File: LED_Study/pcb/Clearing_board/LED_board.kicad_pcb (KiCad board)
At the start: 2 copper layers, 8 x 8 mm, 4 parts

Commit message: new boards
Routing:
- added copper zone on F.Cu, net /GND
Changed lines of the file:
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@@
   (segment (start 102.5 100) (end 102.5 102.05) (width 0.5) (layer "F.Cu") (net 4))
   (via (at 102.5 100) (size 1.4) (drill 0.8) (layers "F.Cu" "B.Cu") (net 4))
+  (zone (net 4) (net_name "/GND") (layer "F.Cu") (hatch edge 0.5)
+    (connect_pads (clearance 0.5))
+    (min_thickness 0.25) (filled_areas_thickness no)
+    (fill yes (thermal_gap 0.5) (thermal_bridge_width 0.5))
+    (polygon
+      (pts
+        (xy 96 96)
+        (xy 104 96)
+        (xy 104 104)
+        (xy 96 104)
+      )
+    )
+  )
 )

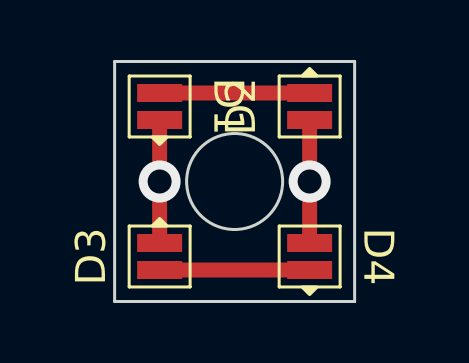
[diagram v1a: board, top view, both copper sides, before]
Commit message: updated boards and ordered from PCBway
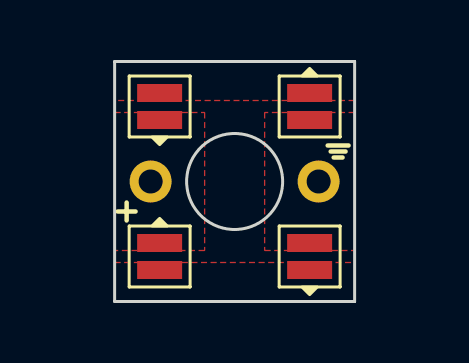
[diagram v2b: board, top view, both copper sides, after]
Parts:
- added J1: Conn_01x01_Pin, Connector_PinHeader_1.00mm:PinHeader_1x01_P1.00mm_Vertical, F.Cu at (97.2, 100.0)
- added J2: Conn_01x01_Pin, Connector_PinHeader_1.00mm:PinHeader_1x01_P1.00mm_Vertical, F.Cu at (102.8, 100.0)
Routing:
- net Net-(D3-K): track 5.00 -> 0.00 mm
- net Net-(D1-K): track 5.00 -> 0.00 mm
- net /Vin: track 4.10 -> 0.00 mm, vias 1 -> 0
- net /GND: track 4.10 -> 0.00 mm, vias 1 -> 0
- added copper zone on F.Cu, net /Vin
- added copper zone on F.Cu, net Net-(D1-K)
- added copper zone on F.Cu, net Net-(D3-K)
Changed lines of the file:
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@@
   (net 3 "/Vin")
   (net 4 "/GND")
+  (footprint "Connector_PinHeader_1.00mm:PinHeader_1x01_P1.00mm_Vertical" (layer "F.Cu")
+    (at 102.8 100)
+    (descr "Through hole straight pin header, 1x01, 1.00mm pitch, single row")
+    (tags "Through hole pin header THT 1x01 1.00mm single row")
+    (property "Sheetfile" "LED_board.kicad_sch")
+    (property "Sheetname" "")
+    (property "ki_description" "Generic connector, single row, 01x01, script generated")
+    (property "ki_keywords" "connector")
+    (attr through_hole)
+    (fp_text reference "J2" (at 0 -1.56) (layer "F.SilkS") hide
+        (effects (font (size 1 1) (thickness 0.15)))
+    )
+    (fp_text value "Conn_01x01_Pin" (at 0 1.56) (layer "F.Fab")
+        (effects (font (size 1 1) (thickness 0.15)))
+    )
+    (fp_text user "${REFERENCE}" (at 0 0 90) (layer "F.Fab")
+        (effects (font (size 0.76 0.76) (thickness 0.114)))
+    )
+    (fp_line (start -1.15 -1) (end -1.15 1)
+      (stroke (width 0.05) (type solid)) (layer "F.CrtYd"))
+    (fp_line (start -1.15 1) (end 1.15 1)
+      (stroke (width 0.05) (type solid)) (layer "F.CrtYd"))
+    (fp_line (start 1.15 -1) (end -1.15 -1)
+      (stroke (width 0.05) (type solid)) (layer "F.CrtYd"))
+    (fp_line (start 1.15 1) (end 1.15 -1)
+      (stroke (width 0.05) (type solid)) (layer "F.CrtYd"))
+    (fp_line (start -0.635 -0.1825) (end -0.3175 -0.5)
+      (stroke (width 0.1) (type solid)) (layer "F.Fab"))
+    (fp_line (start -0.635 0.5) (end -0.635 -0.1825)
+      (stroke (width 0.1) (type solid)) (layer "F.Fab"))
+    (fp_line (start -0.3175 -0.5) (end 0.635 -0.5)
+      (stroke (width 0.1) (type solid)) (layer "F.Fab"))
+    (fp_line (start 0.635 -0.5) (end 0.635 0.5)
+      (stroke (width 0.1) (type solid)) (layer "F.Fab"))
+    (fp_line (start 0.635 0.5) (end -0.635 0.5)
+      (stroke (width 0.1) (type solid)) (layer "F.Fab"))
+    (pad "1" thru_hole circle (at 0 0) (size 1.4 1.4) (drill 0.8) (layers "*.Cu" "*.Mask")
+      (net 4 "/GND") (pinfunction "Pin_1") (pintype "passive"))
+    (model "${KICAD6_3DMODEL_DIR}/Connector_PinHeader_1.00mm.3dshapes/PinHeader_1x01_P1.00mm_Vertical.wrl"
+      (offset (xyz 0 0 0))
+      (scale (xyz 1 1 1))
+      (rotate (xyz 0 0 0))
+    )
+  )
   (footprint "SST-10-IRD-B130-S940:XQE" (layer "F.Cu")
     (at 97.5 102.5 90)
@@
     (property "ki_keywords" "LED diode")
     (attr smd)
-    (fp_text reference "D3" (at 0 -2.286 90 unlocked) (layer "F.SilkS")
+    (fp_text reference "D3" (at 0 -2.286 90 unlocked) (layer "F.SilkS") hide
         (effects (font (size 1 1) (thickness 0.1)))
     )
@@
     (property "ki_keywords" "LED diode")
     (attr smd)
-    (fp_text reference "D1" (at 0 -2.286 -90 unlocked) (layer "F.SilkS")
+    (fp_text reference "D1" (at 0 -2.286 -90 unlocked) (layer "F.SilkS") hide
         (effects (font (size 1 1) (thickness 0.1)))
     )
@@
     (property "ki_keywords" "LED diode")
     (attr smd)
-    (fp_text reference "D4" (at 0 -2.286 -90 unlocked) (layer "F.SilkS")
+    (fp_text reference "D4" (at 0 -2.286 -90 unlocked) (layer "F.SilkS") hide
         (effects (font (size 1 1) (thickness 0.1)))
     )
@@
     (property "ki_keywords" "LED diode")
     (attr smd)
-    (fp_text reference "D2" (at 0 -2.286 90 unlocked) (layer "F.SilkS")
+    (fp_text reference "D2" (at 0 -2.286 90 unlocked) (layer "F.SilkS") hide
         (effects (font (size 1 1) (thickness 0.1)))
     )
@@
       (net 1 "Net-(D1-K)") (pinfunction "A") (pintype "passive") (solder_mask_margin 0.102))
   )
+  (footprint "Connector_PinHeader_1.00mm:PinHeader_1x01_P1.00mm_Vertical" (layer "F.Cu")
+    (at 97.2 100)
+    (descr "Through hole straight pin header, 1x01, 1.00mm pitch, single row")
+    (tags "Through hole pin header THT 1x01 1.00mm single row")
+    (property "Sheetfile" "LED_board.kicad_sch")
+    (property "Sheetname" "")
+    (property "ki_description" "Generic connector, single row, 01x01, script generated")
+    (property "ki_keywords" "connector")
+    (attr through_hole)
+    (fp_text reference "J1" (at 0 -1.56) (layer "F.SilkS") hide
+        (effects (font (size 1 1) (thickness 0.15)))
+    )
+    (fp_text value "Conn_01x01_Pin" (at 0 1.56) (layer "F.Fab")
+        (effects (font (size 1 1) (thickness 0.15)))
+    )
+    (fp_text user "${REFERENCE}" (at 0 0 90) (layer "F.Fab")
+        (effects (font (size 0.76 0.76) (thickness 0.114)))
+    )
+    (fp_line (start -1.15 -1) (end -1.15 1)
+      (stroke (width 0.05) (type solid)) (layer "F.CrtYd"))
+    (fp_line (start -1.15 1) (end 1.15 1)
+      (stroke (width 0.05) (type solid)) (layer "F.CrtYd"))
+    (fp_line (start 1.15 -1) (end -1.15 -1)
+      (stroke (width 0.05) (type solid)) (layer "F.CrtYd"))
+    (fp_line (start 1.15 1) (end 1.15 -1)
+      (stroke (width 0.05) (type solid)) (layer "F.CrtYd"))
+    (fp_line (start -0.635 -0.1825) (end -0.3175 -0.5)
+      (stroke (width 0.1) (type solid)) (layer "F.Fab"))
+    (fp_line (start -0.635 0.5) (end -0.635 -0.1825)
+      (stroke (width 0.1) (type solid)) (layer "F.Fab"))
+    (fp_line (start -0.3175 -0.5) (end 0.635 -0.5)
+      (stroke (width 0.1) (type solid)) (layer "F.Fab"))
+    (fp_line (start 0.635 -0.5) (end 0.635 0.5)
+      (stroke (width 0.1) (type solid)) (layer "F.Fab"))
+    (fp_line (start 0.635 0.5) (end -0.635 0.5)
+      (stroke (width 0.1) (type solid)) (layer "F.Fab"))
+    (pad "1" thru_hole circle (at 0 0) (size 1.4 1.4) (drill 0.8) (layers "*.Cu" "*.Mask")
+      (net 3 "/Vin") (pinfunction "Pin_1") (pintype "passive"))
+    (model "${KICAD6_3DMODEL_DIR}/Connector_PinHeader_1.00mm.3dshapes/PinHeader_1x01_P1.00mm_Vertical.wrl"
+      (offset (xyz 0 0 0))
+      (scale (xyz 1 1 1))
+      (rotate (xyz 0 0 0))
+    )
+  )
+  (gr_line (start 103.7 99) (end 103.2 99)
+    (stroke (width 0.15) (type default)) (layer "F.SilkS"))
+  (gr_line (start 103.3 99.2) (end 103.6 99.2)
+    (stroke (width 0.15) (type default)) (layer "F.SilkS"))
+  (gr_line (start 96.1 101) (end 96.7 101)
+    (stroke (width 0.15) (type default)) (layer "F.SilkS"))
+  (gr_line (start 96.4 100.7) (end 96.4 101.3)
+    (stroke (width 0.15) (type default)) (layer "F.SilkS"))
+  (gr_line (start 103.1 98.8) (end 103.8 98.8)
+    (stroke (width 0.15) (type default)) (layer "F.SilkS"))
   (gr_circle (center 100 100) (end 101.6 100)
     (stroke (width 0.1) (type default)) (fill none) (layer "Edge.Cuts"))
   (gr_rect (start 96 96) (end 104 104)
     (stroke (width 0.1) (type default)) (fill none) (layer "Edge.Cuts"))
-  (segment (start 97.5 97.05) (end 102.5 97.05) (width 0.5) (layer "F.Cu") (net 1))
-  (segment (start 97.5 102.95) (end 102.5 102.95) (width 0.5) (layer "F.Cu") (net 2))
-  (segment (start 97.5 102.05) (end 97.5 100) (width 0.5) (layer "F.Cu") (net 3))
-  (segment (start 97.5 97.95) (end 97.5 100) (width 0.5) (layer "F.Cu") (net 3))
-  (via (at 97.5 100) (size 1.4) (drill 0.8) (layers "F.Cu" "B.Cu") (net 3))
-  (segment (start 102.5 97.95) (end 102.5 100) (width 0.5) (layer "F.Cu") (net 4))
-  (segment (start 102.5 100) (end 102.5 102.05) (width 0.5) (layer "F.Cu") (net 4))
-  (via (at 102.5 100) (size 1.4) (drill 0.8) (layers "F.Cu" "B.Cu") (net 4))
-  (zone (net 4) (net_name "/GND") (layer "F.Cu") (hatch edge 0.5)
+  (zone (net 2) (net_name "Net-(D3-K)") (layer "F.Cu") (hatch edge 0.5)
+    (priority 2)
     (connect_pads (clearance 0.5))
     (min_thickness 0.25) (filled_areas_thickness no)
-    (fill yes (thermal_gap 0.5) (thermal_bridge_width 0.5))
+    (fill yes (thermal_gap 0.25) (thermal_bridge_width 0.5))
     (polygon
       (pts
+        (xy 96 102.7)
+        (xy 104 102.7)
+        (xy 104 104)
+        (xy 96 104)
+      )
+    )
+  )
+  (zone (net 4) (net_name "/GND") (layer "F.Cu") (hatch edge 0.5)
+    (priority 3)
+    (connect_pads (clearance 0.5))
+    (min_thickness 0.25) (filled_areas_thickness no)
+    (fill yes (thermal_gap 0.25) (thermal_bridge_width 0.5))
+    (polygon
+      (pts
+        (xy 104 102.3)
+        (xy 104 97.7)
+        (xy 101 97.7)
+        (xy 101 102.3)
+      )
+    )
+  )
+  (zone (net 1) (net_name "Net-(D1-K)") (layer "F.Cu") (hatch edge 0.5)
+    (priority 1)
+    (connect_pads (clearance 0.5))
+    (min_thickness 0.25) (filled_areas_thickness no)
+    (fill yes (thermal_gap 0.25) (thermal_bridge_width 0.5))
+    (polygon
+      (pts
+        (xy 96 97.3)
         (xy 96 96)
         (xy 104 96)
-        (xy 104 104)
-        (xy 96 104)
-      )
-    )
+        (xy 104 97.3)
+      )
+    )
+  )
+  (zone (net 3) (net_name "/Vin") (layer "F.Cu") (hatch edge 0.5)
+    (connect_pads (clearance 0.25))
+    (min_thickness 0.25) (filled_areas_thickness no)
+    (fill yes (thermal_gap 0.25) (thermal_bridge_width 0.5))
+    (polygon
+      (pts
+        (xy 96 97.7)
+        (xy 99 97.7)
+        (xy 99 102.3)
+        (xy 96 102.3)
+      )
+    )
